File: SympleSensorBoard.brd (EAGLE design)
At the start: 50.8 x 50.8 mm, 45 parts, among them IC1 STM32F303K8T6, SW1 B2B-XH-A_LF__SN_, SW2 B2B-XH-A_LF__SN_, SW3 B2B-XH-A_LF__SN_, SW4 B2B-XH-A_LF__SN_, SW5 B2B-XH-A_LF__SN_, SW6 B2B-XH-A_LF__SN_, SW7 B2B-XH-A_LF__SN_, Y1 CSTCE12M0G55-R0

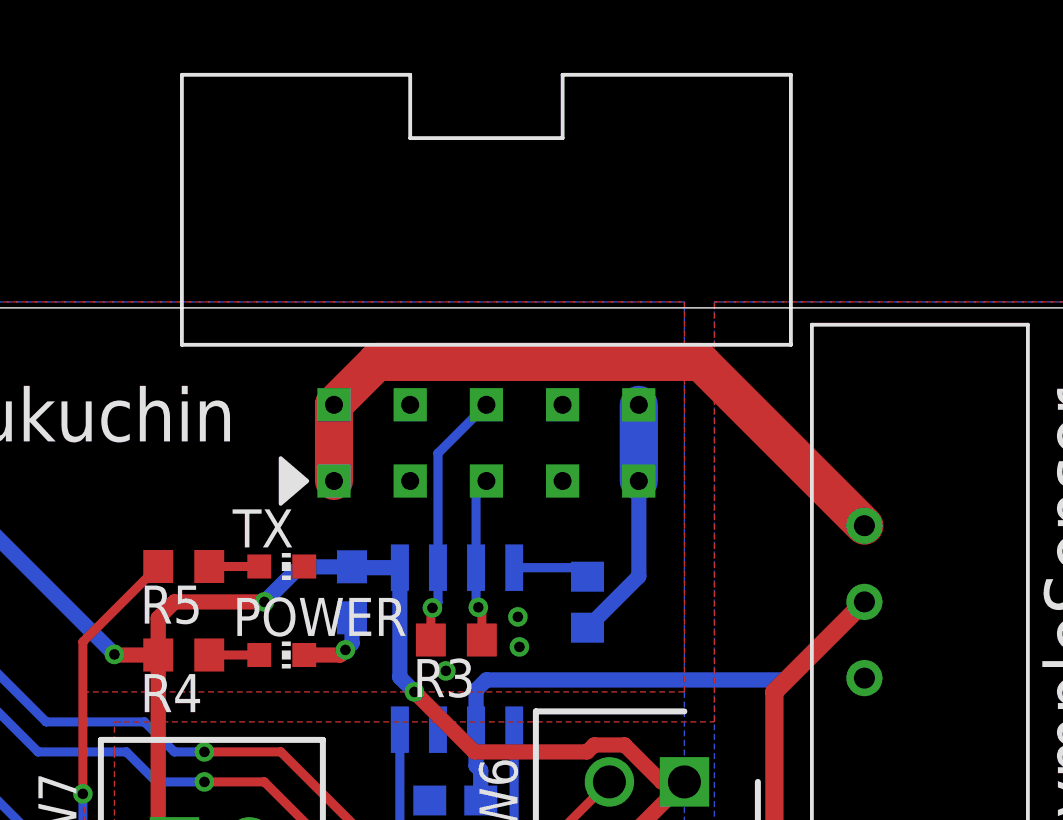
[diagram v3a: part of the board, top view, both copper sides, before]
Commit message: 10ピンコネクタのホールの大きさを修正した
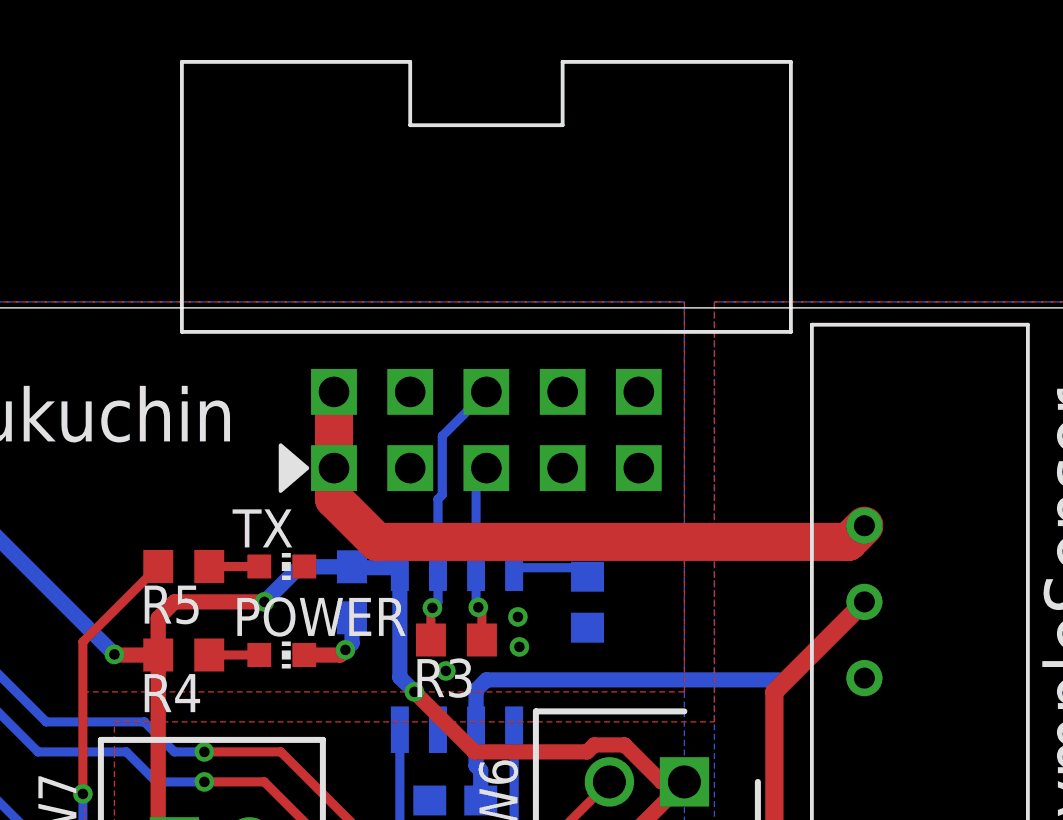
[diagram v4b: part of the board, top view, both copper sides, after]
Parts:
- removed BOX10P-L1: BOX10PBOX10P-L, user_conector:BOX10P-L
- added U$4: BOX10PBOX10P-L, user_conector:BOX10P-L
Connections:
- net +12V: now also U$4.P$1, U$4.P$2; no longer BOX10P-L1.P$1, BOX10P-L1.P$2
- net +5V: now also U$4.P$10, U$4.P$9; no longer BOX10P-L1.P$10, BOX10P-L1.P$9
- net CAN_H: now also U$4.P$5; no longer BOX10P-L1.P$5
- net CAN_L: now also U$4.P$6; no longer BOX10P-L1.P$6
- net GND: now also U$4.P$7, U$4.P$8; no longer BOX10P-L1.P$7, BOX10P-L1.P$8
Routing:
- net +5V: track 8.34 -> 0.00 mm
- net +12V: track 23.1 -> 22.1 mm
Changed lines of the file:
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@@
 </autorouter>
 <elements>
-<element name="BOX10P-L1" library="user_conector" package="BOX10P-L" value="BOX10PBOX10P-L" x="25.4" y="47.57" smashed="yes" rot="R180"/>
 <element name="C1" library="rcl" library_urn="urn:adsk.eagle:library:334" package="C0603" package3d_urn="urn:adsk.eagle:package:23616/2" value="0.1μ" x="20.92" y="41.32" smashed="yes" rot="MR90">
 <attribute name="NAME" x="19.555" y="37.685" size="1.27" layer="26" rot="MR90"/>
@@
 <attribute name="RS_PRICE-STOCK" value="http://uk.rs-online.com/web/p/products/8201554P" x="15" y="33" size="1.778" layer="27" display="off"/>
 </element>
+<element name="U$4" library="user_conector" package="BOX10P-L" value="BOX10PBOX10P-L" x="25.4" y="48" smashed="yes" rot="R180"/>
 </elements>
 <signals>
@@
 <contactref element="U$3" pad="7"/>
 <contactref element="U$3" pad="11"/>
-<contactref element="BOX10P-L1" pad="P$7"/>
-<contactref element="BOX10P-L1" pad="P$8"/>
 <contactref element="ADC_1" pad="2"/>
 <contactref element="R7" pad="1"/>
@@
 <wire x1="35" y1="38" x2="38" y2="41" width="0.6096" layer="1"/>
 <wire x1="35" y1="33.562" x2="35" y2="38" width="0.6096" layer="1"/>
+<contactref element="U$4" pad="P$7"/>
+<contactref element="U$4" pad="P$8"/>
 </signal>
 <signal name="OSC_IN">
@@
 </signal>
 <signal name="+12V">
-<contactref element="BOX10P-L1" pad="P$2"/>
-<contactref element="BOX10P-L1" pad="P$1"/>
 <contactref element="U$1" pad="P$1"/>
-<wire x1="20.32" y1="45.03" x2="20.32" y2="47.57" width="1.27" layer="1"/>
-<wire x1="21.75" y1="49" x2="20.32" y2="47.57" width="1.27" layer="1"/>
-<wire x1="38" y1="43.54" x2="32.54" y2="49" width="1.27" layer="1"/>
-<wire x1="32.54" y1="49" x2="21.75" y2="49" width="1.27" layer="1"/>
+<wire x1="38" y1="43.54" x2="37.46" y2="43" width="1.27" layer="1"/>
+<wire x1="37.46" y1="43" x2="21.75" y2="43" width="1.27" layer="1"/>
+<contactref element="U$4" pad="P$1"/>
+<contactref element="U$4" pad="P$2"/>
+<wire x1="21.75" y1="43" x2="20.32" y2="44.43" width="1.27" layer="1"/>
+<wire x1="20.32" y1="44.43" x2="20.32" y2="45.46" width="1.27" layer="1"/>
+<wire x1="20.32" y1="45.46" x2="20.32" y2="48" width="1.27" layer="1"/>
 </signal>
 <signal name="+5V">
@@
 <contactref element="C4" pad="1"/>
 <contactref element="R2" pad="2"/>
-<contactref element="BOX10P-L1" pad="P$10"/>
-<contactref element="BOX10P-L1" pad="P$9"/>
 <contactref element="ADC_1" pad="1"/>
 <contactref element="ADC_2" pad="1"/>
@@
 <contactref element="ADC_6" pad="1"/>
 <contactref element="ADC_7" pad="1"/>
-<wire x1="30.48" y1="47.57" x2="30.48" y2="45.03" width="1.27" layer="16"/>
-<wire x1="30.48" y1="45.03" x2="30.48" y2="41.85" width="0.508" layer="16"/>
-<wire x1="30.48" y1="41.85" x2="28.77" y2="40.14" width="0.508" layer="16"/>
-<wire x1="28.77" y1="40.14" x2="28.63" y2="40" width="0.508" layer="16"/>
 <polygon width="0.1524" layer="16">
 <vertex x="32" y="33"/>
@@
 <vertex x="11" y="33"/>
 </polygon>
+<contactref element="U$4" pad="P$10"/>
+<contactref element="U$4" pad="P$9"/>
 </signal>
 <signal name="N$2">
@@
 <contactref element="U$2" pad="P$7"/>
 <contactref element="R3" pad="1"/>
-<contactref element="BOX10P-L1" pad="P$5"/>
-<wire x1="25.055" y1="42.14" x2="25.055" y2="44.685" width="0.3048" layer="16"/>
-<wire x1="25.055" y1="44.685" x2="25.4" y2="45.03" width="0.3048" layer="16"/>
 <wire x1="25.055" y1="42.14" x2="25.055" y2="40.895" width="0.3048" layer="16"/>
 <wire x1="25.055" y1="40.895" x2="25.131125" y2="40.818875" width="0.3048" layer="16"/>
@@
 <wire x1="25.131125" y1="40.818875" x2="25.25" y2="40.7" width="0.3048" layer="1"/>
 <wire x1="25.25" y1="40.7" x2="25.25" y2="39.73" width="0.3048" layer="1"/>
+<contactref element="U$4" pad="P$5"/>
+<wire x1="25.055" y1="42.14" x2="25.055" y2="45.115" width="0.3048" layer="16"/>
+<wire x1="25.055" y1="45.115" x2="25.4" y2="45.46" width="0.3048" layer="16"/>
 </signal>
 <signal name="CAN_L">
 <contactref element="R3" pad="2"/>
 <contactref element="U$2" pad="P$6"/>
-<contactref element="BOX10P-L1" pad="P$6"/>
-<wire x1="23.785" y1="42.14" x2="23.785" y2="45.955" width="0.3048" layer="16"/>
-<wire x1="23.785" y1="45.955" x2="25.4" y2="47.57" width="0.3048" layer="16"/>
 <wire x1="23.6" y1="40.8" x2="23.55" y2="40.75" width="0.3048" layer="1"/>
 <wire x1="23.55" y1="40.75" x2="23.55" y2="39.73" width="0.3048" layer="1"/>
@@
 <wire x1="23.785" y1="42.14" x2="23.785" y2="40.985" width="0.3048" layer="16"/>
 <wire x1="23.785" y1="40.985" x2="23.6" y2="40.8" width="0.3048" layer="16"/>
+<contactref element="U$4" pad="P$6"/>
+<wire x1="23.785" y1="42.14" x2="23.785" y2="44.42395" width="0.3048" layer="16"/>
+<wire x1="23.785" y1="44.42395" x2="23.9298" y2="44.56875" width="0.3048" layer="16"/>
+<wire x1="23.9298" y1="46.5298" x2="25.4" y2="48" width="0.3048" layer="16"/>
+<wire x1="23.9298" y1="44.56875" x2="23.9298" y2="46.5298" width="0.3048" layer="16"/>
 </signal>
 <signal name="N$3">
